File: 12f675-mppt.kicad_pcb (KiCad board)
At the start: 2 copper layers, 97.6 x 76.8 mm, 45 parts, among them IC1 PIC12F629-I/P, J1 S+, J2 S-, J3 O+, J4 O-, Q1 BUK9511-55A127, Q2 BUK9511-55A127, Q3 2N2222A, Q4 2N2222A, Q5 2N2907A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

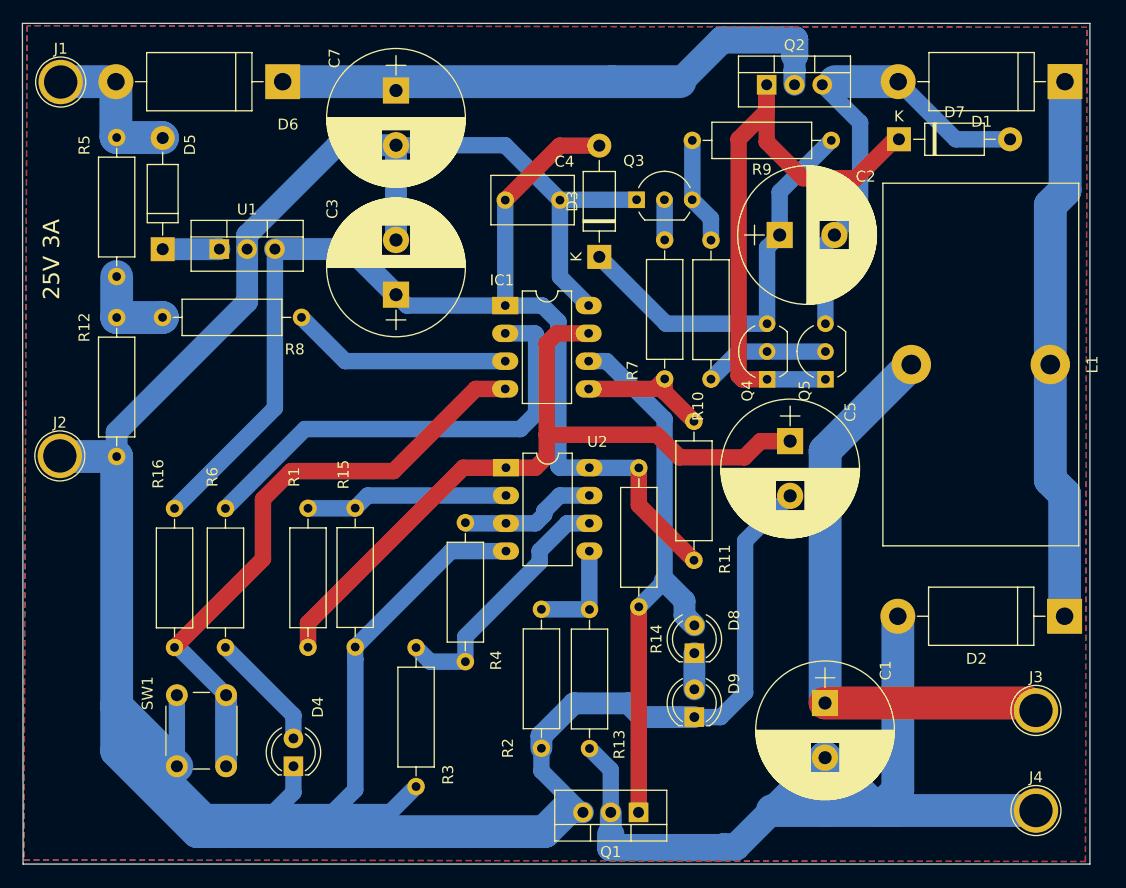
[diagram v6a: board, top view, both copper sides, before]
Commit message: Fix circuit. R1 -> 1k
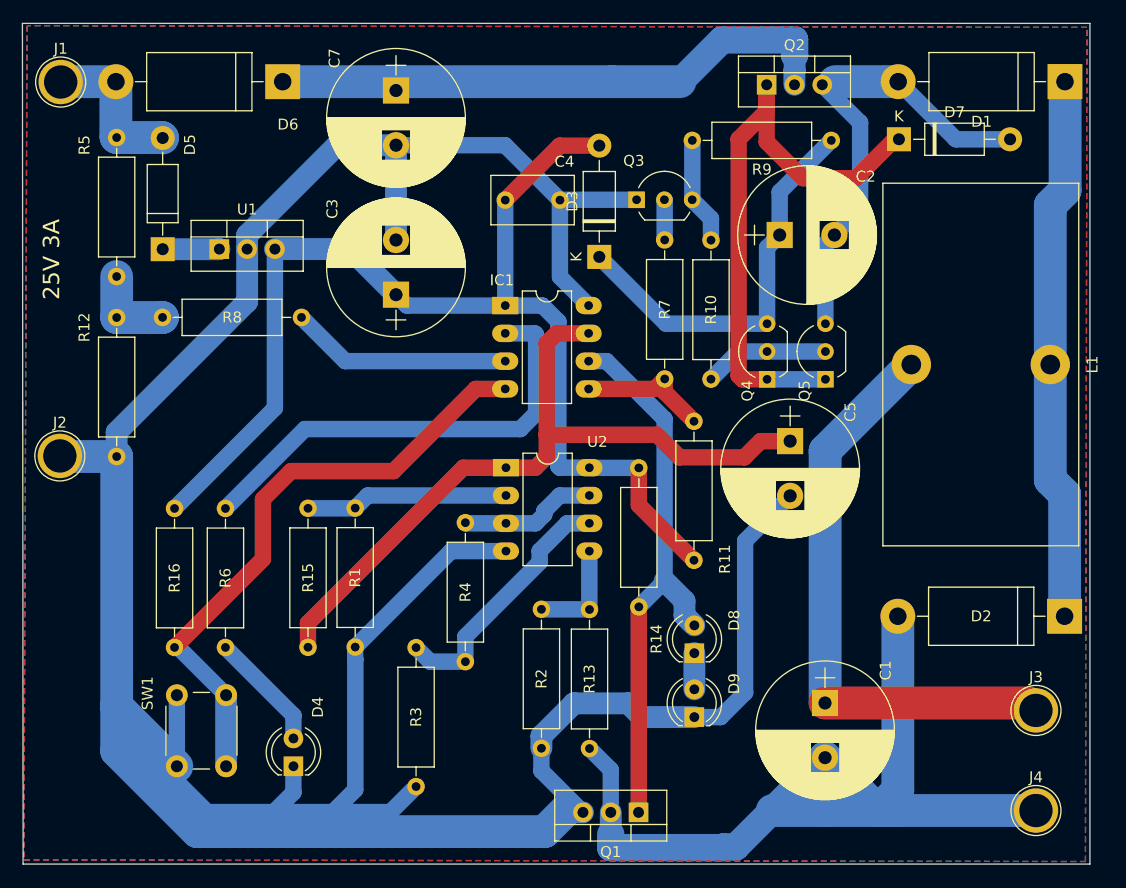
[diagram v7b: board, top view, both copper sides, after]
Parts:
- R1: value 10k -> 1k
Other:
- net class Default removed
